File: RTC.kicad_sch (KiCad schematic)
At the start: 14 parts, among them J7 Molex 470531000, U10 EMC2301-1-ACZL-TR, U11 74LVC1G07SE-7, U9 PCF85063AT/AAZ, Y2 X32K768S301

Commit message: worked some more on converting components (unfinished)
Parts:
- removed BT1: Battery_Cell, Battery:BatteryHolder_Keystone_3034_1x20mm, symbol Device:Battery_Cell
- removed D3: BAT54C-7-F, Package_TO_SOT_SMD:SOT-23, symbol Diode:BAT54C
- U9: value PCF85063AT/AAZ -> PCF85063AT; Field6 PCF85063AT/AAZ -> PCF85063AT
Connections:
- net +3.3v is gone; now on net +3.3V: C21.1, R16.2, U10.3 (VDD)
- net +3.3V: now reaches C20.1, U9.8 (VDD)
- net +12v renamed +12V
- net +5v renamed +5V
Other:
- moved on the sheet: C20, C21, U10, U9, Y2

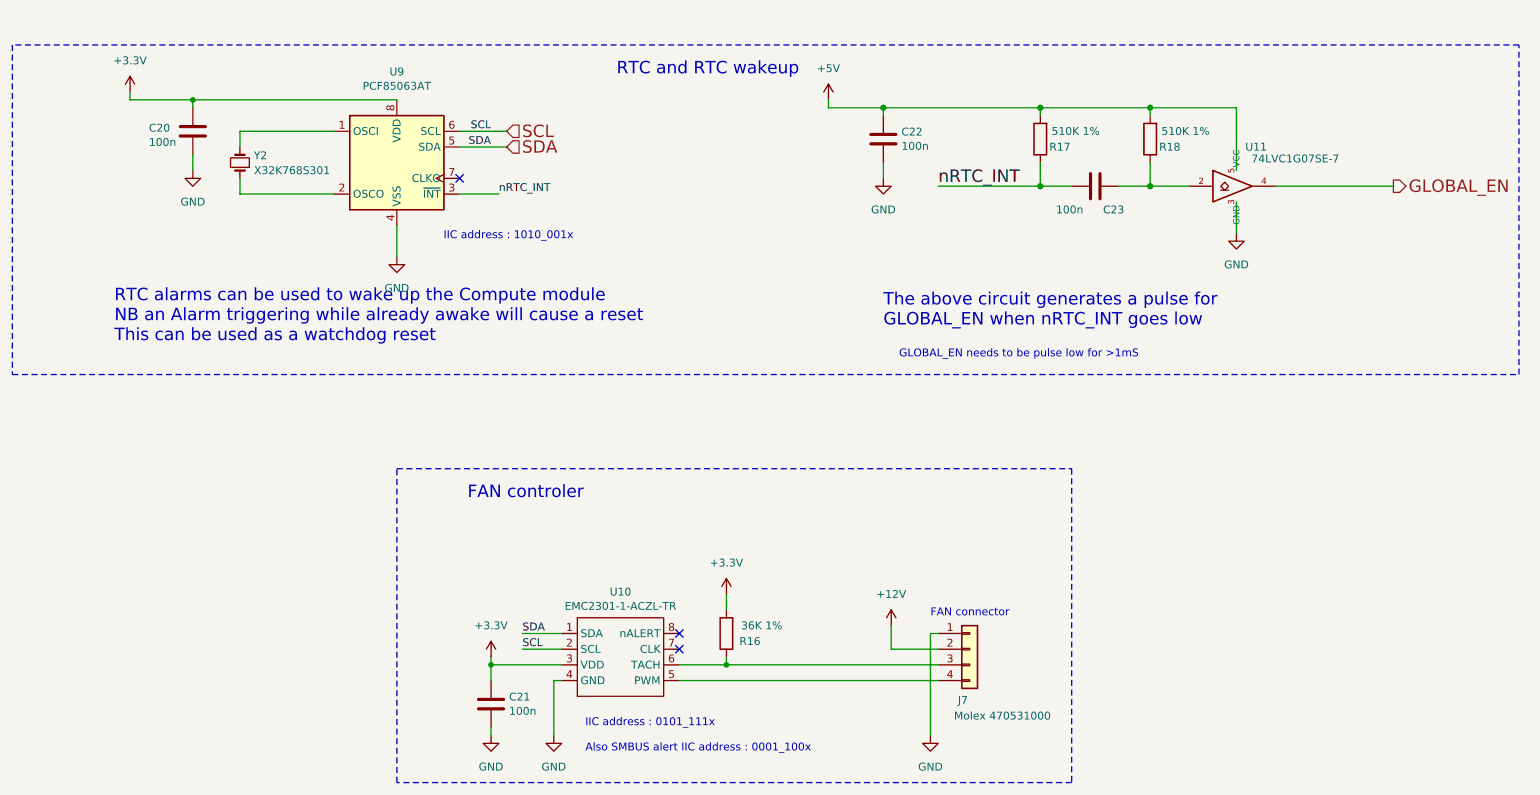
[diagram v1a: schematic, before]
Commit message: power dist, hdmi, and rtc are done; finding a new usb hub
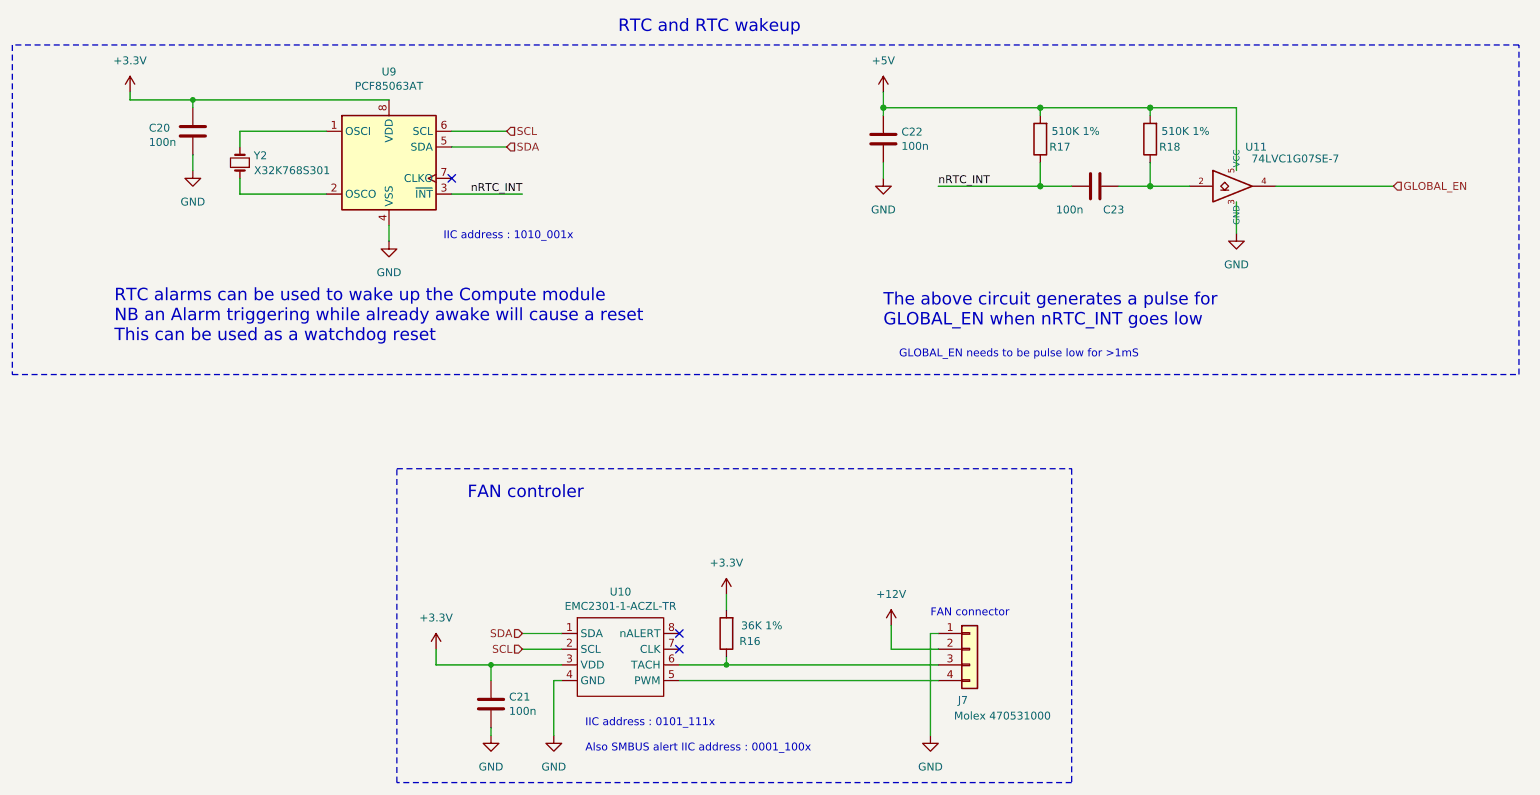
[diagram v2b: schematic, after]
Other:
- moved on the sheet: U9
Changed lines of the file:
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@@
 	)
 	(no_connect
-		(at 93.98 55.88)
+		(at 92.71 55.88)
 	)
 	(wire
@@
 	(wire
 		(pts
-			(xy 153.67 44.45) (xy 162.56 44.45)
-		)
-		(stroke
-			(width 0)
-			(type solid)
-		)
-	)
-	(wire
-		(pts
 			(xy 187.96 44.45) (xy 187.96 45.72)
 		)
@@
 	(wire
 		(pts
-			(xy 58.42 48.26) (xy 73.66 48.26)
+			(xy 58.42 48.26) (xy 72.39 48.26)
 		)
 		(stroke
@@
 	(wire
 		(pts
-			(xy 58.42 58.42) (xy 73.66 58.42)
-		)
-		(stroke
-			(width 0)
-			(type solid)
+			(xy 58.42 58.42) (xy 72.39 58.42)
+		)
+		(stroke
+			(width 0)
+			(type solid)
+		)
+	)
+	(wire
+		(pts
+			(xy 90.17 134.62) (xy 99.06 134.62)
+		)
+		(stroke
+			(width 0)
+			(type default)
 		)
 	)
@@
 	(wire
 		(pts
-			(xy 93.98 48.26) (xy 101.6 48.26)
+			(xy 92.71 48.26) (xy 101.6 48.26)
 		)
 		(stroke
@@
 	(wire
 		(pts
-			(xy 50.8 43.18) (xy 83.82 43.18)
-		)
-		(stroke
-			(width 0)
-			(type solid)
-		)
-	)
-	(wire
-		(pts
-			(xy 93.98 50.8) (xy 101.6 50.8)
-		)
-		(stroke
-			(width 0)
-			(type solid)
-		)
-	)
-	(wire
-		(pts
-			(xy 99.06 133.35) (xy 99.06 134.62)
+			(xy 50.8 43.18) (xy 82.55 43.18)
+		)
+		(stroke
+			(width 0)
+			(type solid)
+		)
+	)
+	(wire
+		(pts
+			(xy 92.71 50.8) (xy 101.6 50.8)
+		)
+		(stroke
+			(width 0)
+			(type solid)
+		)
+	)
+	(wire
+		(pts
+			(xy 90.17 132.08) (xy 90.17 134.62)
 		)
 		(stroke
@@
 	(wire
 		(pts
-			(xy 83.82 63.5) (xy 83.82 68.58)
+			(xy 82.55 63.5) (xy 82.55 66.04)
 		)
 		(stroke
@@
 	(wire
 		(pts
-			(xy 153.67 43.18) (xy 153.67 44.45)
+			(xy 162.56 41.91) (xy 162.56 44.45)
 		)
 		(stroke
@@
 	(wire
 		(pts
-			(xy 93.98 58.42) (xy 100.33 58.42)
+			(xy 92.71 58.42) (xy 104.14 58.42)
 		)
 		(stroke
@@
 	(text "RTC and RTC wakeup"
 		(exclude_from_sim no)
-		(at 119.38 39.37 0)
+		(at 119.634 32.512 0)
 		(effects
 			(font
@@
 		(exclude_from_sim no)
 		(at 114.3 144.78 0)
-		(effects
-			(font
-				(size 1.27 1.27)
-			)
-			(justify left bottom)
-		)
-	)
-	(label "SDA"
-		(at 104.14 129.54 0)
-		(fields_autoplaced yes)
-		(effects
-			(font
-				(size 1.27 1.27)
-			)
-			(justify left bottom)
-		)
-	)
-	(label "nRTC_INT"
-		(at 100.33 58.42 0)
-		(fields_autoplaced yes)
-		(effects
-			(font
-				(size 1.27 1.27)
-			)
-			(justify left bottom)
-		)
-	)
-	(label "SCL"
-		(at 104.14 132.08 0)
-		(fields_autoplaced yes)
 		(effects
 			(font
@@
 		(effects
 			(font
-				(size 2.0066 2.0066)
+				(size 1.27 1.27)
 			)
 			(justify left bottom)
 		)
 	)
-	(label "SDA"
-		(at 99.06 50.8 180)
+	(label "nRTC_INT"
+		(at 104.14 58.42 180)
 		(fields_autoplaced yes)
 		(effects
@@
 		)
 	)
-	(label "SCL"
-		(at 99.06 48.26 180)
+	(hierarchical_label "SDA"
+		(shape input)
+		(at 104.14 129.54 180)
 		(fields_autoplaced yes)
 		(effects
@@
 				(size 1.27 1.27)
 			)
-			(justify right bottom)
+			(justify right)
+		)
+	)
+	(hierarchical_label "SCL"
+		(shape input)
+		(at 104.14 132.08 180)
+		(fields_autoplaced yes)
+		(effects
+			(font
+				(size 1.27 1.27)
+			)
+			(justify right)
+		)
+	)
+	(hierarchical_label "GLOBAL_EN"
+		(shape input)
+		(at 245.11 57.15 0)
+		(fields_autoplaced yes)
+		(effects
+			(font
+				(size 1.27 1.27)
+			)
+			(justify left)
 		)
 	)
@@
 		(effects
 			(font
-				(size 2.0066 2.0066)
+				(size 1.27 1.27)
 			)
 			(justify left)
@@
 		(effects
 			(font
-				(size 2.0066 2.0066)
-			)
-			(justify left)
-		)
-	)
-	(hierarchical_label "GLOBAL_EN"
-		(shape output)
-		(at 245.11 57.15 0)
-		(fields_autoplaced yes)
-		(effects
-			(font
-				(size 2.0066 2.0066)
+				(size 1.27 1.27)
 			)
 			(justify left)
@@
 	(symbol
 		(lib_id "power:+3.3V")
-		(at 99.06 133.35 0)
+		(at 90.17 132.08 0)
 		(unit 1)
 		(exclude_from_sim no)
@@
 		(fields_autoplaced yes)
 		(property "Reference" "#PWR0100"
-			(at 99.06 137.16 0)
+			(at 90.17 135.89 0)
 			(effects
 				(font
@@
 		)
 		(property "Value" "+3.3V"
-			(at 99.06 128.27 0)
+			(at 90.17 127 0)
 			(effects
 				(font
@@
 		)
 		(property "Footprint" ""
-			(at 99.06 133.35 0)
+			(at 90.17 132.08 0)
 			(effects
 				(font
@@
 		)
 		(property "Datasheet" ""
-			(at 99.06 133.35 0)
+			(at 90.17 132.08 0)
 			(effects
 				(font
@@
 		)
 		(property "Description" "Power symbol creates a global label with name \"+3.3V\""
-			(at 99.06 133.35 0)
+			(at 90.17 132.08 0)
 			(effects
 				(font
@@
 	(symbol
 		(lib_id "Timer_RTC:PCF8563T")
-		(at 83.82 53.34 0)
+		(at 82.55 53.34 0)
 		(unit 1)
 		(exclude_from_sim no)
@@
 		(dnp no)
 		(property "Reference" "U9"
-			(at 83.82 38.6334 0)
+			(at 82.55 38.6334 0)
 			(effects
 				(font
@@
 		)
 		(property "Value" "PCF85063AT"
-			(at 83.82 40.9448 0)
+			(at 82.55 40.9448 0)
 			(effects
 				(font
@@
 		)
 		(property "Footprint" "Package_SO:SOIC-8_3.9x4.9mm_P1.27mm"
-			(at 83.82 53.34 0)
+			(at 82.55 53.34 0)
 			(effects
 				(font
@@
 		)
 		(property "Datasheet" "https://www.nxp.com/docs/en/data-sheet/PCF85063A.pdf"
-			(at 83.82 53.34 0)
+			(at 82.55 53.34 0)
 			(effects
 				(font
@@
 		)
 		(property "Description" ""
-			(at 83.82 53.34 0)
+			(at 82.55 53.34 0)
 			(effects
 				(font
@@
 		)
 		(property "Field4" "Farnell"
-			(at 83.82 53.34 0)
+			(at 82.55 53.34 0)
 			(effects
 				(font
@@
 		)
 		(property "Field5" "2890042"
-			(at 83.82 53.34 0)
+			(at 82.55 53.34 0)
 			(effects
 				(font
@@
 		)
 		(property "Field7" "NXP"
-			(at 83.82 53.34 0)
+			(at 82.55 53.34 0)
 			(effects
 				(font
@@
 		)
 		(property "Field6" "PCF85063AT"
-			(at 83.82 53.34 0)
+			(at 82.55 53.34 0)
 			(effects
 				(font
@@
 		)
 		(property "Part Description" "Real Time Clock (RTC) IC Clock/Calendar I²C, 2-Wire Serial 8-SOIC (0.154\", 3.90mm Width)"
-			(at 83.82 53.34 0)
+			(at 82.55 53.34 0)
 			(effects
 				(font
@@
 		(lib_name "GND_4")
 		(lib_id "power:GND")
-		(at 83.82 68.58 0)
+		(at 82.55 66.04 0)
 		(unit 1)
 		(exclude_from_sim no)
@@
 		(fields_autoplaced yes)
 		(property "Reference" "#PWR044"
-			(at 83.82 74.93 0)
+			(at 82.55 72.39 0)
 			(effects
 				(font
@@
 		)
 		(property "Value" "GND"
-			(at 83.82 73.66 0)
+			(at 82.55 71.12 0)
 			(effects
 				(font
@@
 		)
 		(property "Footprint" ""
-			(at 83.82 68.58 0)
+			(at 82.55 66.04 0)
 			(effects
 				(font
@@
 		)
 		(property "Datasheet" ""
-			(at 83.82 68.58 0)
+			(at 82.55 66.04 0)
 			(effects
 				(font
@@
 		)
 		(property "Description" "Power symbol creates a global label with name \"GND\" , ground"
-			(at 83.82 68.58 0)
+			(at 82.55 66.04 0)
 			(effects
 				(font
@@
 	(symbol
 		(lib_id "power:+5V")
-		(at 153.67 43.18 0)
+		(at 162.56 41.91 0)
 		(unit 1)
 		(exclude_from_sim no)
@@
 		(fields_autoplaced yes)
 		(property "Reference" "#PWR049"
-			(at 153.67 46.99 0)
+			(at 162.56 45.72 0)
 			(effects
 				(font
@@
 		)
 		(property "Value" "+5V"
-			(at 153.67 38.1 0)
+			(at 162.56 36.83 0)
 			(effects
 				(font
@@
 		)
 		(property "Footprint" ""
-			(at 153.67 43.18 0)
+			(at 162.56 41.91 0)
 			(effects
 				(font
@@
 		)
 		(property "Datasheet" ""
-			(at 153.67 43.18 0)
+			(at 162.56 41.91 0)
 			(effects
 				(font
@@
 		)
 		(property "Description" "Power symbol creates a global label with name \"+5V\""
-			(at 153.67 43.18 0)
-			(effects
-				(font
+			(at 162.56 41.91 0)
+			(effects
+				(font

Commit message: made more changes
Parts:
- removed U9: PCF85063AT, Package_SO:SOIC-8_3.9x4.9mm_P1.27mm, symbol Timer_RTC:PCF8563T
- added U1: PCF8563T, Package_SO:SOIC-8_3.9x4.9mm_P1.27mm, symbol Timer_RTC:PCF8563T
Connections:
- net GND: now also U1.4 (VSS)
- net SCL: now also U1.6 (SCL)
- net SDA: now also U1.5 (SDA)
- net nRTC_INT: now also U1.3 (~{INT})
- net at Y2.2: now also U1.1 (OSCI)
- net at Y2.1: now also U1.2 (OSCO)
- net +12V renamed +12V_PWR
- net +3.3V renamed +3.3V_PWR
- net +3.3V_PWR: now also U1.8 (VDD)
- net +5V renamed +5V_PWR

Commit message: finished USB i think, working on general gpio in more detail
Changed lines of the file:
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@@
+		(color 0 0 0 0)
+	)
+	(junction
+		(at 93.98 119.38)
+		(diameter 0)
 		(color 0 0 0 0)
 	)
@@
 	(wire
 		(pts
+			(xy 93.98 114.3) (xy 93.98 119.38)
+		)
+		(stroke
+			(width 0)
+			(type default)
+		)
+	)
+	(wire
+		(pts
 			(xy 187.96 44.45) (xy 187.96 45.72)
 		)
@@
 	(wire
 		(pts
+			(xy 154.94 44.45) (xy 162.56 44.45)
+		)
+		(stroke
+			(width 0)
+			(type default)
+		)
+	)
+	(wire
+		(pts
 			(xy 219.71 59.69) (xy 219.71 64.77)
 		)
@@
 	(wire
 		(pts
-			(xy 40.64 38.1) (xy 40.64 43.18)
-		)
-		(stroke
-			(width 0)
-			(type default)
-		)
-	)
-	(wire
-		(pts
 			(xy 187.96 57.15) (xy 187.96 53.34)
 		)
@@
 		)
 	)
-	(wire
-		(pts
-			(xy 90.17 123.19) (xy 90.17 134.62)
-		)
-		(stroke
-			(width 0)
-			(type default)
-		)
-	)
 	(polyline
 		(pts
@@
 	(wire
 		(pts
-			(xy 90.17 134.62) (xy 99.06 134.62)
+			(xy 93.98 119.38) (xy 93.98 134.62)
+		)
+		(stroke
+			(width 0)
+			(type default)
+		)
+	)
+	(wire
+		(pts
+			(xy 93.98 119.38) (xy 137.16 119.38)
+		)
+		(stroke
+			(width 0)
+			(type default)
+		)
+	)
+	(wire
+		(pts
+			(xy 93.98 134.62) (xy 99.06 134.62)
 		)
 		(stroke
@@
 	(wire
 		(pts
-			(xy 162.56 39.37) (xy 162.56 44.45)
-		)
-		(stroke
-			(width 0)
-			(type default)
-		)
-	)
-	(wire
-		(pts
 			(xy 92.71 48.26) (xy 101.6 48.26)
 		)
@@
 	(wire
 		(pts
-			(xy 40.64 43.18) (xy 50.8 43.18)
+			(xy 36.83 43.18) (xy 50.8 43.18)
 		)
 		(stroke
@@
 	(hierarchical_label "+5V_PWR"
 		(shape input)
-		(at 162.56 39.37 180)
+		(at 154.94 44.45 180)
 		(fields_autoplaced yes)
 		(effects
@@
 	(hierarchical_label "+3.3V_PWR"
 		(shape input)
-		(at 90.17 123.19 0)
-		(fields_autoplaced yes)
-		(effects
-			(font
-				(size 1.27 1.27)
-			)
-			(justify left)
-		)
-	)
-	(hierarchical_label "+3.3V_PWR"
-		(shape input)
-		(at 137.16 119.38 0)
+		(at 93.98 114.3 0)
 		(fields_autoplaced yes)
 		(effects
@@
 	(hierarchical_label "+3.3V_PWR"
 		(shape input)
-		(at 40.64 38.1 180)
-		(fields_autoplaced yes)
-		(effects
+		(at 36.83 43.18 180)
+		(fields_autoplaced yes)
+		(effects

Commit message: we ballin??
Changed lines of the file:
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@@
 			)
 		)
-		(property "Description" ""
+		(property "Description" "Two pin crystal, small symbol"
 			(at 58.42 53.34 0)
 			(effects
@@
 			)
 		)
-		(property "Datasheet" "https://ww1.microchip.com/downloads/en/DeviceDoc/2301.pdf"
+		(property "Datasheet" "https://ww1.microchip.com/downloads/aemDocuments/documents/MSLD/ProductDocuments/DataSheets/EMC2301-2-3-5-Data-Sheet-DS20006532A.pdf"
 			(at 121.92 139.7 0)
 			(effects
@@
 			)
 		)
-		(property "Datasheet" "https://www.molex.com/pdm_docs/sd/470531000_sd.pdf"
+		(property "Datasheet" "~"
 			(at 176.53 132.08 0)
 			(effects
@@
 			)
 		)
-		(property "Description" ""
+		(property "Description" "Generic connector, single row, 01x04, script generated (kicad-library-utils/schlib/autogen/connector/)"
 			(at 176.53 132.08 0)
 			(effects
